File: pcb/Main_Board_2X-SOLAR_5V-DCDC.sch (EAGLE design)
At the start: 69 parts, among them CN5 USBA_FEMALE, M3AB FDMC8030, M4 SI7611DN, M5 FDMC8327L, T2 MMUN2133LT1G, U1 LTC4015EUHFPBFQFN-38_UHF-M, U3 TPS61090RSAR, X1 6V_PV

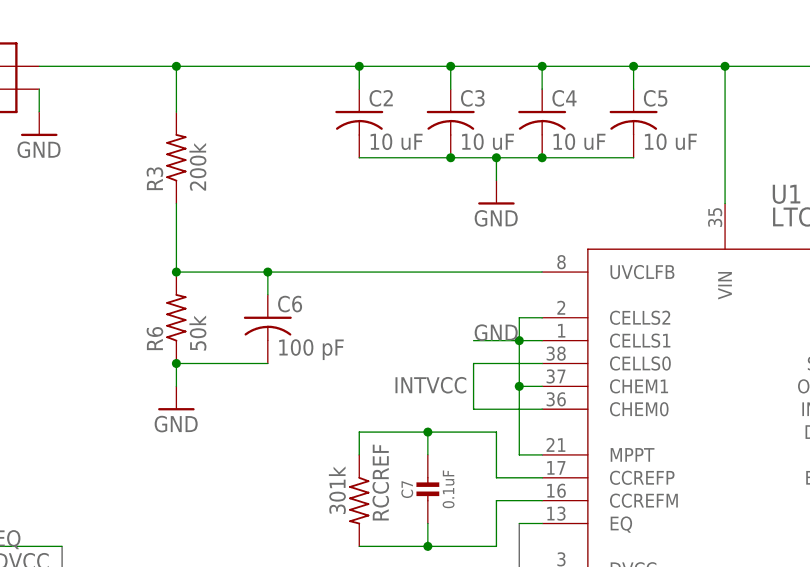
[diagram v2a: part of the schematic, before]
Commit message: Updated schematic with UVCLFB input
added 10k resistor
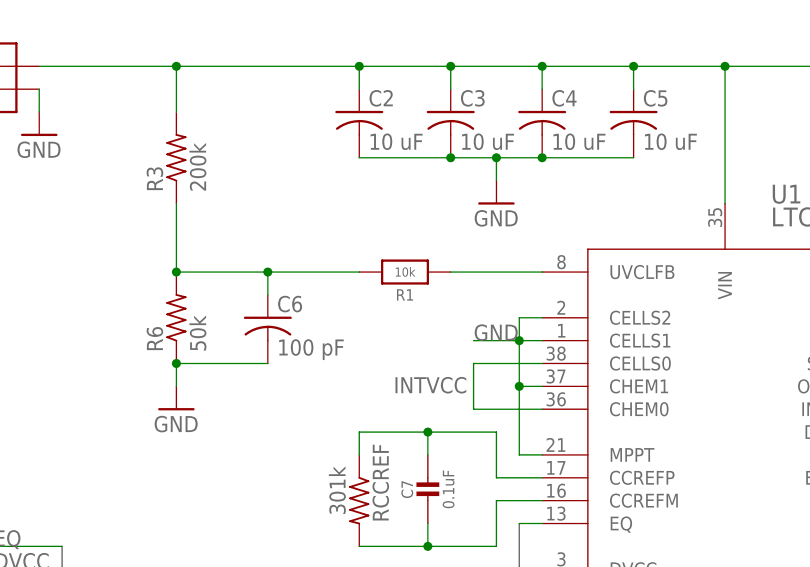
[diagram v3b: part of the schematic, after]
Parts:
- added R1: 10k, microbuilder:RESISTOR_0805MP
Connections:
- new net N$5: R1.1, U1.UVCLFB
- net UVCLFB: now also R1.2; no longer U1.UVCLFB
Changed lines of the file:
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@@
 <part name="CN1" library="adafruit" library_urn="urn:adsk.eagle:library:420" deviceset="JST_2PIN" device="-THM"/>
 <part name="U$12" library="microbuilder" deviceset="GND" device=""/>
+<part name="R1" library="microbuilder" deviceset="RESISTOR" device="_0805MP" value="10k"/>
 </parts>
 <sheets>
@@
 <instance part="CN1" gate="G$1" x="236.22" y="45.72"/>
 <instance part="U$12" gate="G$1" x="226.06" y="40.64"/>
+<instance part="R1" gate="G$1" x="60.96" y="129.54" rot="R180"/>
 </instances>
 <busses>
@@
 <pinref part="C6" gate="G$1" pin="1"/>
 <wire x1="45.72" y1="129.54" x2="45.72" y2="127" width="0.1524" layer="91"/>
-<pinref part="U1" gate="A" pin="UVCLFB"/>
-<wire x1="76.2" y1="129.54" x2="45.72" y2="129.54" width="0.1524" layer="91"/>
 <pinref part="R6" gate="G$1" pin="2"/>
 <wire x1="45.72" y1="129.54" x2="35.56" y2="129.54" width="0.1524" layer="91"/>
-<junction x="45.72" y="129.54"/>
 <junction x="35.56" y="129.54"/>
 <pinref part="R3" gate="G$1" pin="1"/>
 <wire x1="35.56" y1="129.54" x2="35.56" y2="137.16" width="0.1524" layer="91"/>
+<pinref part="R1" gate="G$1" pin="2"/>
+<wire x1="45.72" y1="129.54" x2="55.88" y2="129.54" width="0.1524" layer="91"/>
+<junction x="45.72" y="129.54"/>
 </segment>
 </net>
@@
 </segment>
 </net>
+<net name="N$5" class="0">
+<segment>
+<pinref part="R1" gate="G$1" pin="1"/>
+<pinref part="U1" gate="A" pin="UVCLFB"/>
+<wire x1="66.04" y1="129.54" x2="76.2" y2="129.54" width="0.1524" layer="91"/>
+</segment>
+</net>

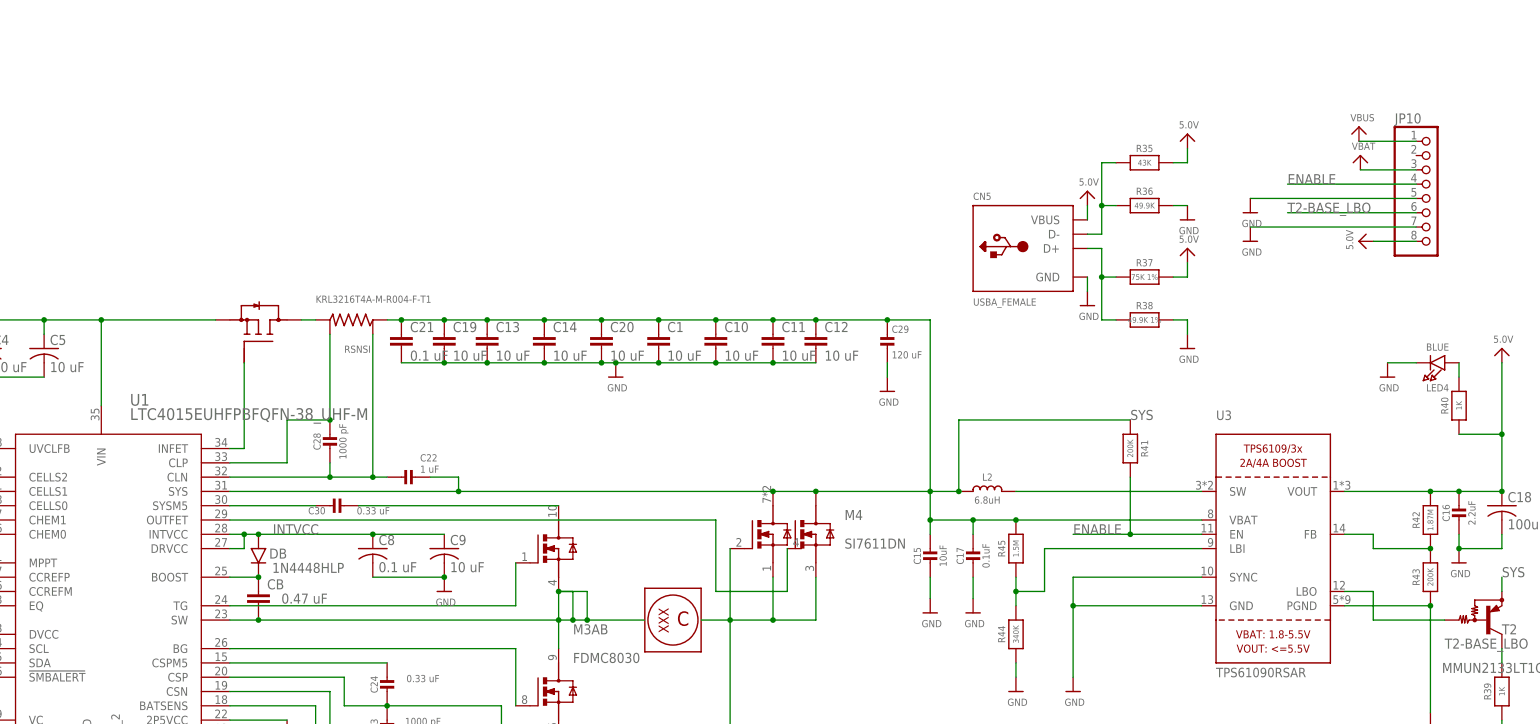
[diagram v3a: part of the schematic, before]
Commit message: Updates to schematic and board layout to fix V1
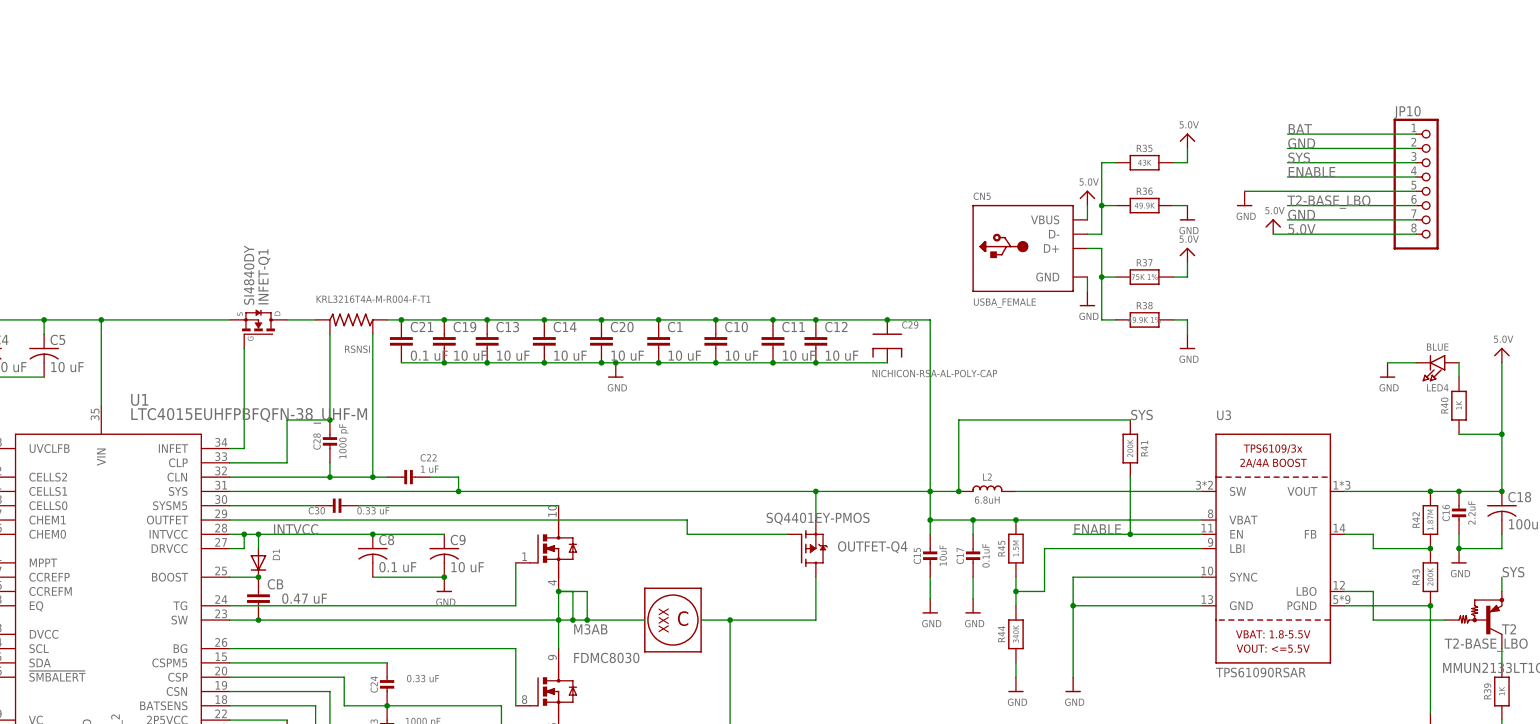
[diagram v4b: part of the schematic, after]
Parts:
- removed DB: 1N4448HLP, RCT:1N4448HLP
- removed M4: SI7611DN, Si7611DN:SI7611DN
- removed M5: FDMC8327L, RCT:FDMC8327L
- added D1: (no value), adafruit:DIODESOD-123
- added INFET-Q1: SI4840DY, TRANS_SI7635DP-T1-GE3:SI4840DY
- added OUTFET-Q4: SQ4401EY-PMOS, TRANS_SI7635DP-T1-GE3:SQ4401EY-PMOS
- C29: value 120 uF -> NICHICON-RSA-AL-POLY-CAP; device microbuilder:CAP_CERAMIC0805-NOOUTLINE -> RCT:NICHICON-RSA-AL-POLY-CAP
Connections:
- removed net OUTFET: M4.G2, U1.OUTFET
- removed net VBUS: JP10.1
- new net N$10: OUTFET-Q4.G, U1.OUTFET
- net BAT: now also JP10.1
- net GND: now also C29.P$1, JP10.2; no longer C29.1
- net INFET: now also INFET-Q1.G; no longer M5.GATE
- net INTVCC: now also D1.A; no longer DB.P$2
- net N$13: now also D1.C; no longer DB.P$1
- net N$3: now also INFET-Q1.D; no longer M5.DRAIN
- net OUTFET_M4_SOURCE: now also OUTFET-Q4.D; no longer M4.G1, M4.S1, M4.S2
- net SYS: now also C29.P$2, OUTFET-Q4.S; no longer C29.2, M4.D1, M4.D2
- net VIN: now also INFET-Q1.S; no longer M5.SOURCE
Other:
- moved on the sheet: C29, JP10

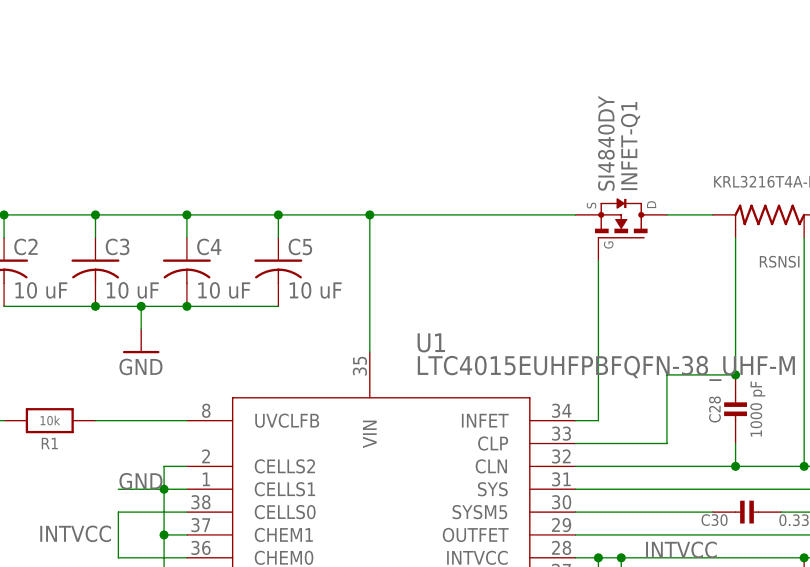
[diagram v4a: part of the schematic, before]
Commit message: Updated schematic and board layout for V1
Added jumper for VIN and updated footprint for 8030 package
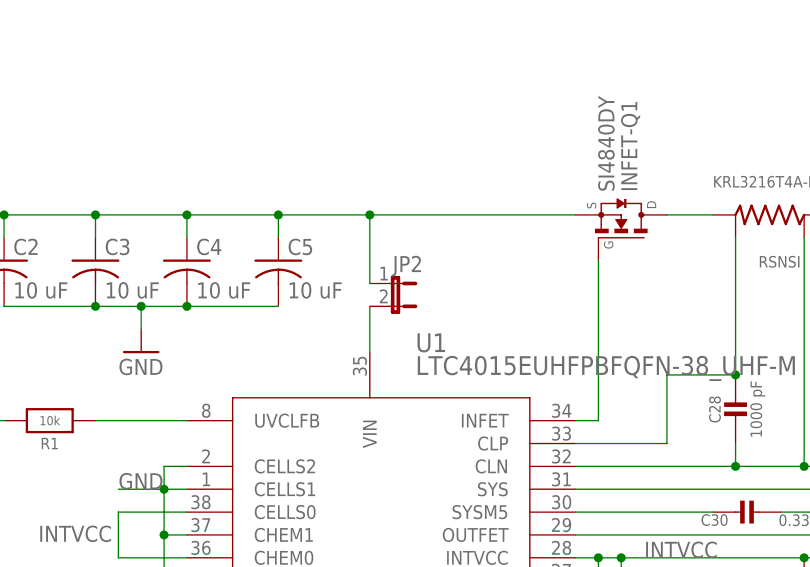
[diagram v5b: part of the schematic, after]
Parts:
- added JP2: (no value), jumper:JP1E
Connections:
- new net N$12: JP2.2, U1.VIN
- net VIN: now also JP2.1; no longer U1.VIN
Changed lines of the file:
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@@
 <part name="OUTFET-Q4" library="TRANS_SI7635DP-T1-GE3" deviceset="SQ4401EY-PMOS" device=""/>
 <part name="INFET-Q1" library="TRANS_SI7635DP-T1-GE3" deviceset="SI4840DY" device=""/>
+<part name="JP2" library="jumper" library_urn="urn:adsk.eagle:library:252" deviceset="JP1E" device="" package3d_urn="urn:adsk.eagle:package:15455/1"/>
 </parts>
 <sheets>
@@
 </instance>
 <instance part="INFET-Q1" gate="G$1" x="124.46" y="152.4" rot="MR90"/>
+<instance part="JP2" gate="A" x="99.06" y="144.78" rot="R270"/>
 </instances>
 <busses>
@@
 <wire x1="86.36" y1="152.4" x2="96.52" y2="152.4" width="0.1524" layer="91"/>
 <junction x="86.36" y="152.4"/>
-<pinref part="U1" gate="A" pin="VIN"/>
-<wire x1="96.52" y1="152.4" x2="96.52" y2="137.16" width="0.1524" layer="91"/>
+<wire x1="96.52" y1="152.4" x2="96.52" y2="144.78" width="0.1524" layer="91"/>
 <wire x1="119.38" y1="152.4" x2="96.52" y2="152.4" width="0.1524" layer="91"/>
 <junction x="96.52" y="152.4"/>
@@
 <junction x="35.56" y="152.4"/>
 <pinref part="INFET-Q1" gate="G$1" pin="S"/>
+<pinref part="JP2" gate="A" pin="1"/>
 </segment>
 </net>
@@
 </segment>
 </net>
+<net name="N$12" class="0">
+<segment>
+<pinref part="U1" gate="A" pin="VIN"/>
+<pinref part="JP2" gate="A" pin="2"/>
+<wire x1="96.52" y1="142.24" x2="96.52" y2="137.16" width="0.1524" layer="91"/>
+</segment>
+</net>
 </nets>
 </sheet>
@@
 with this version.
 </note>
+<note version="8.3" severity="warning">
+Since Version 8.3, EAGLE supports URNs for individual library
+assets (packages, symbols, and devices). The URNs of those assets
+will not be understood (or retained) with this version.
+</note>
+<note version="8.3" severity="warning">
+Since Version 8.3, EAGLE supports the association of 3D packages
+with devices in libraries, schematics, and board files. Those 3D
+packages will not be understood (or retained) with this version.
+</note>
 </compatibility>

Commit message: OSH print V1 P2
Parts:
- added C31: 2.2 nF, adafruit:C-USC0805
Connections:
- net N$5: now also C6.1
- net UVCLFB: now also C31.2; no longer C6.1
- net VIN: now also C31.1
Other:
- moved on the sheet: C6, R1
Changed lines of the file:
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@@
 <part name="INFET-Q1" library="TRANS_SI7635DP-T1-GE3" deviceset="SI4840DY" device=""/>
 <part name="JP2" library="jumper" library_urn="urn:adsk.eagle:library:252" deviceset="JP1E" device="" package3d_urn="urn:adsk.eagle:package:15455/1"/>
+<part name="C31" library="adafruit" library_urn="urn:adsk.eagle:library:420" deviceset="C-US" device="C0805" value="2.2 nF"/>
 </parts>
 <sheets>
@@
 <instance part="C4" gate="G$1" x="76.2" y="147.32"/>
 <instance part="C5" gate="G$1" x="86.36" y="147.32"/>
-<instance part="C6" gate="G$1" x="45.72" y="124.46"/>
+<instance part="C6" gate="G$1" x="58.42" y="124.46"/>
 <instance part="R6" gate="G$1" x="35.56" y="124.46" rot="R90"/>
 <instance part="GND3" gate="1" x="35.56" y="114.3"/>
@@
 <instance part="CN1" gate="G$1" x="236.22" y="45.72"/>
 <instance part="U$12" gate="G$1" x="226.06" y="40.64"/>
-<instance part="R1" gate="G$1" x="60.96" y="129.54" rot="R180"/>
+<instance part="R1" gate="G$1" x="50.8" y="129.54" rot="R180"/>
 <instance part="C29" gate="G$1" x="236.22" y="147.32" smashed="yes">
 <attribute name="NAME" x="238.76" y="150.876" size="1.27" layer="95" font="vector"/>
@@
 <instance part="INFET-Q1" gate="G$1" x="124.46" y="152.4" rot="MR90"/>
 <instance part="JP2" gate="A" x="99.06" y="144.78" rot="R270"/>
+<instance part="C31" gate="G$1" x="45.72" y="142.24"/>
 </instances>
 <busses>
@@
 <pinref part="GND3" gate="1" pin="GND"/>
 <pinref part="C6" gate="G$1" pin="2"/>
-<wire x1="45.72" y1="119.38" x2="35.56" y2="119.38" width="0.1524" layer="91"/>
+<wire x1="58.42" y1="119.38" x2="35.56" y2="119.38" width="0.1524" layer="91"/>
 <junction x="35.56" y="119.38"/>
 <wire x1="35.56" y1="119.38" x2="35.56" y2="116.84" width="0.1524" layer="91"/>
@@
 <net name="UVCLFB" class="0">
 <segment>
-<pinref part="C6" gate="G$1" pin="1"/>
-<wire x1="45.72" y1="129.54" x2="45.72" y2="127" width="0.1524" layer="91"/>
 <pinref part="R6" gate="G$1" pin="2"/>
 <wire x1="45.72" y1="129.54" x2="35.56" y2="129.54" width="0.1524" layer="91"/>
@@
 <wire x1="35.56" y1="129.54" x2="35.56" y2="137.16" width="0.1524" layer="91"/>
 <pinref part="R1" gate="G$1" pin="2"/>
-<wire x1="45.72" y1="129.54" x2="55.88" y2="129.54" width="0.1524" layer="91"/>
+<pinref part="C31" gate="G$1" pin="2"/>
+<wire x1="45.72" y1="137.16" x2="45.72" y2="129.54" width="0.1524" layer="91"/>
 <junction x="45.72" y="129.54"/>
 </segment>
@@
 <junction x="55.88" y="152.4"/>
 <pinref part="R3" gate="G$1" pin="2"/>
-<wire x1="35.56" y1="152.4" x2="55.88" y2="152.4" width="0.1524" layer="91"/>
+<wire x1="35.56" y1="152.4" x2="45.72" y2="152.4" width="0.1524" layer="91"/>
+<wire x1="45.72" y1="152.4" x2="55.88" y2="152.4" width="0.1524" layer="91"/>
 <wire x1="35.56" y1="147.32" x2="35.56" y2="152.4" width="0.1524" layer="91"/>
 <junction x="35.56" y="152.4"/>
 <pinref part="INFET-Q1" gate="G$1" pin="S"/>
 <pinref part="JP2" gate="A" pin="1"/>
+<pinref part="C31" gate="G$1" pin="1"/>
+<wire x1="45.72" y1="144.78" x2="45.72" y2="152.4" width="0.1524" layer="91"/>
+<junction x="45.72" y="152.4"/>
 </segment>
 </net>
@@
 <pinref part="R1" gate="G$1" pin="1"/>
 <pinref part="U1" gate="A" pin="UVCLFB"/>
-<wire x1="66.04" y1="129.54" x2="76.2" y2="129.54" width="0.1524" layer="91"/>
-</segment>
-</net>
+<wire x1="55.88" y1="129.54" x2="58.42" y2="129.54" width="0.1524" layer="91"/>
+<pinref part="C6" gate="G$1" pin="1"/>
+<wire x1="58.42" y1="129.54" x2="76.2" y2="129.54" width="0.1524" layer="91"/>
+<wire x1="58.42" y1="127" x2="58.42" y2="129.54" width="0.1524" layer="91"/>
+<junction x="58.42" y="129.54"/>
+</segment>
+</net>

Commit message: Fixed NTC resistor routing
Added 10k NTC resistor to NTC pin and added INTVCC output to jumpers. Updated silkscreens for easier reading
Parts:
- removed JP2: (no value), jumper:JP1E
- removed U$4: XAL1010-103ME-103ME, RCT:XAL1010-103ME-103ME
- added L1: XAL1010-103ME-103ME, RCT:XAL1010-103ME-103ME
- added RNTC: 10k, microbuilder:RESISTOR_0805MP
- C31: value 2.2 nF -> 2200 pF
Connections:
- net GND: now also RNTC.1; no longer RNTCBIAS.1, U1.NTC
- net N$12: now also RNTC.2, RNTCBIAS.1, U1.NTC; no longer JP2.2, U1.VIN
- net OUTFET_M4_SOURCE: now also L1.P$2; no longer U$4.P$2
- net SW_LTC: now also L1.P$1; no longer U$4.P$1
- net VIN: now also U1.VIN; no longer JP2.1
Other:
- moved on the sheet: C1, C10, C11, C12, C13, C14, C15, C16, C17, C18, C19, C2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
